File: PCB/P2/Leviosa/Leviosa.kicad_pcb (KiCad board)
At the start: 2 copper layers, 50 parts, among them J1 Barrel_Jack, J2 2.54mm 1x03 Spare

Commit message: finish initial pcb layout
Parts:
- moved H2 128.0 mm to (88.0, 67.0)
- moved H3 98.0 mm to (82.5, 118.5)
- moved H1 70.7 mm to (136.0, 100.0)
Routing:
- net /V_out: track 76.5 -> 85.2 mm
- net /current_sense: track 53.1 -> 57.6 mm
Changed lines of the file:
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@@
 	(footprint "MountingHole:MountingHole_3.2mm_M3_ISO7380"
 		(layer "F.Cu")
-		(at 157.2 174.65)
+		(at 88 67)
 		(descr "Mounting Hole 3.2mm, M3, no annular, generated by kicad-footprint-generator mountinghole.py")
 		(tags "mountinghole M3 ISO7380")
@@
 	(footprint "MountingHole:MountingHole_3.2mm_M3_ISO7380"
 		(layer "F.Cu")
-		(at 157.2 181.9)
+		(at 82.5 118.5)
 		(descr "Mounting Hole 3.2mm, M3, no annular, generated by kicad-footprint-generator mountinghole.py")
 		(tags "mountinghole M3 ISO7380")
@@
 	(footprint "MountingHole:MountingHole_3.2mm_M3_ISO7380"
 		(layer "F.Cu")
-		(at 157.2 167.4)
+		(at 136 100)
 		(descr "Mounting Hole 3.2mm, M3, no annular, generated by kicad-footprint-generator mountinghole.py")
 		(tags "mountinghole M3 ISO7380")
@@
 		(tags "SOD-123")
 		(property "Reference" "D1"
-			(at -3.7 0 0)
+			(at 0 0 0)
 			(layer "F.SilkS")
 			(effects
@@
 	)
 	(segment
+		(start 68 122.37)
+		(end 75.1 129.47)
+		(width 0.25)
+		(layer "F.Cu")
+		(net 2)
+	)
+	(segment
 		(start 75.5 86.85)
 		(end 72.95 84.3)
@@
 	)
 	(segment
+		(start 62.7 110.9)
+		(end 68 116.2)
+		(width 0.25)
+		(layer "F.Cu")
+		(net 2)
+	)
+	(segment
 		(start 129.38 112.0175)
 		(end 129.05 111.6875)
@@
 	(segment
 		(start 67.4 96.5)
-		(end 62.6 101.3)
+		(end 62.7 101.2)
+		(width 0.25)
+		(layer "F.Cu")
+		(net 2)
+	)
+	(segment
+		(start 62.7 101.2)
+		(end 62.7 110.9)
 		(width 0.25)
 		(layer "F.Cu")
@@
 	)
 	(segment
+		(start 68 116.2)
+		(end 68 122.37)
+		(width 0.25)
+		(layer "F.Cu")
+		(net 2)
+	)
+	(segment
 		(start 83.625 124.97)
 		(end 83.625 129.47)
@@
 	)
 	(segment
-		(start 74.47 129.47)
+		(start 75.1 129.47)
 		(end 83.625 129.47)
 		(width 0.25)
@@
 	)
 	(segment
-		(start 62.6 117.6)
-		(end 74.47 129.47)
-		(width 0.25)
-		(layer "F.Cu")
-		(net 2)
-	)
-	(segment
 		(start 118.1 129)
 		(end 109.4 137.7)
@@
 	)
 	(segment
-		(start 62.6 101.3)
-		(end 62.6 117.6)
-		(width 0.25)
-		(layer "F.Cu")
-		(net 2)
-	)
-	(segment
 		(start 97.275 137.7)
 		(end 94.085 134.51)
@@
 	)
 	(segment
-		(start 81.2 68.3)
+		(start 67.9 82.8)
+		(end 67.9 78.6)
+		(width 0.25)
+		(layer "F.Cu")
+		(net 9)
+	)
+	(segment
+		(start 81.435 70.1125)
 		(end 81.435 68.535)
 		(width 0.25)
@@
 	)
 	(segment
+		(start 78.2 68.3)
+		(end 67.9 78.6)
+		(width 0.25)
+		(layer "F.Cu")
+		(net 9)
+	)
+	(segment
 		(start 63.35 91.2)
-		(end 63.35 83.15)
+		(end 63.35 87.35)
 		(width 0.25)
 		(layer "F.Cu")
@@
 	)
 	(segment
-		(start 63.35 83.15)
-		(end 78.2 68.3)
+		(start 63.35 87.35)
+		(end 67.9 82.8)
 		(width 0.25)
 		(layer "F.Cu")
@@
 	)
 	(segment
-		(start 78.2 68.3)
-		(end 81.2 68.3)
+		(start 81.2 68.3)
+		(end 78.2 68.3)
 		(width 0.25)
 		(layer "F.Cu")
@@
 	(segment
 		(start 81.435 68.535)
-		(end 81.435 70.1125)
+		(end 81.2 68.3)
 		(width 0.25)
 		(layer "F.Cu")
@@
 	)
 	(segment
+		(start 77.05 120.05)
+		(end 79.2 122.2)
+		(width 0.4)
+		(layer "F.Cu")
+		(net 11)
+	)
+	(segment
+		(start 111.8 122.2)
+		(end 123.5 110.5)
+		(width 0.4)
+		(layer "F.Cu")
+		(net 11)
+	)
+	(segment
 		(start 73.2 116.188748)
 		(end 70.5 116.188748)
@@
 	)
 	(segment
-		(start 77.05 119.8)
-		(end 77.05 115.55)
+		(start 123.5 110.5)
+		(end 123.5 96.9125)
 		(width 0.4)
 		(layer "F.Cu")
@@
 	)
 	(segment
-		(start 126.6 100.8375)
-		(end 126.6 100.0125)
+		(start 77.05 119.8)
+		(end 77.05 115.55)
 		(width 0.4)
 		(layer "F.Cu")
@@
 	)
 	(segment
-		(start 107.6375 119.8)
-		(end 77.05 119.8)
+		(start 126.6 100.8375)
+		(end 126.6 100.0125)
 		(width 0.4)
 		(layer "F.Cu")
@@
 	)
 	(segment
+		(start 79.2 122.2)
+		(end 111.8 122.2)
+		(width 0.4)
+		(layer "F.Cu")
+		(net 11)
+	)
+	(segment
 		(start 73.888748 115.5)
 		(end 73.2 116.188748)
@@
 	)
 	(segment
-		(start 126.6 100.8375)
-		(end 107.6375 119.8)
+		(start 77.05 119.8)
+		(end 77.05 120.05)
 		(width 0.4)
 		(layer "F.Cu")
@@
 	)
 	(segment
-		(start 127.949 109.308274)
-		(end 127.949 108.18819)
+		(start 110.7 125.4)
+		(end 100.655 125.4)
 		(width 0.25)
 		(layer "F.Cu")
@@
 	)
 	(segment
-		(start 128 108.13719)
-		(end 128 103)
+		(start 127.949 109.308274)
+		(end 127.949 108.18819)
 		(width 0.25)
 		(layer "F.Cu")
@@
 	)
 	(segment
-		(start 128 103)
-		(end 127.6 102.6)
+		(start 100.655 125.4)
+		(end 94.085 131.97)
 		(width 0.25)
 		(layer "F.Cu")
@@
 	)
 	(segment
-		(start 127.6 102.6)
-		(end 125.581376 102.6)
+		(start 128 108.13719)
+		(end 128 103)
 		(width 0.25)
 		(layer "F.Cu")
@@
 	)
 	(segment
-		(start 100.655 125.4)
-		(end 94.085 131.97)
+		(start 125 103.4)
+		(end 125 111.1)
 		(width 0.25)
 		(layer "F.Cu")
@@
 	)
 	(segment
-		(start 102.781376 125.4)
-		(end 100.655 125.4)
+		(start 128 103)
+		(end 127.6 102.6)
 		(width 0.25)
 		(layer "F.Cu")
@@
 	)
 	(segment
-		(start 125.581376 102.6)
-		(end 102.781376 125.4)
+		(start 127.6 102.6)
+		(end 125.8 102.6)
 		(width 0.25)
 		(layer "F.Cu")
@@
 	)
 	(segment
+		(start 125 111.1)
+		(end 110.7 125.4)
+		(width 0.25)
+		(layer "F.Cu")
+		(net 23)
+	)
+	(segment
 		(start 127.874 109.383274)
 		(end 127.949 109.308274)
 		(width 0.25)
 		(layer "F.Cu")
+		(net 23)
+	)
+	(segment
+		(start 125.8 102.6)
+		(end 125 103.4)
+		(width 0.25)
+		(layer "F.Cu")

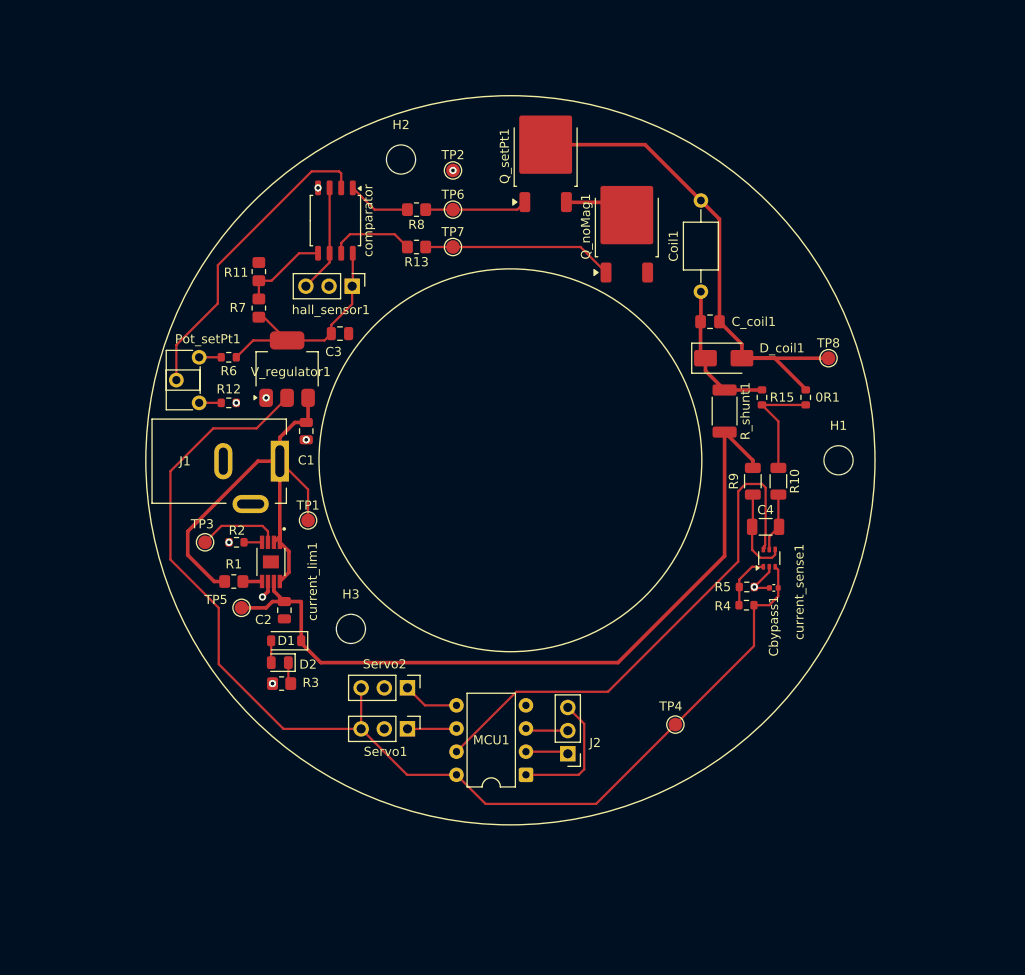
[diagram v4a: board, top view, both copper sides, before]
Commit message: update a resistor and PCB
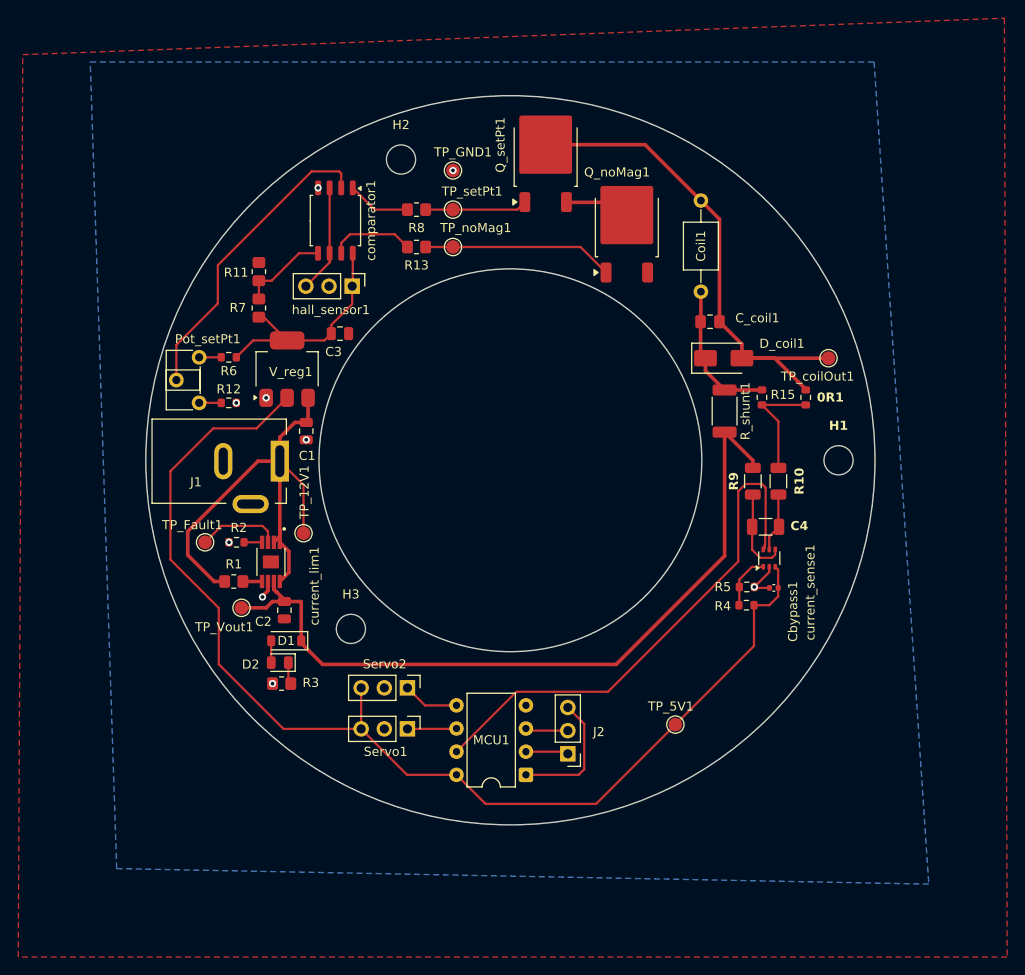
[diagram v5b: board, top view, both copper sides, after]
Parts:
- R11: value 54.2kΩ -> 64.2kΩ
- moved TP_12V1 1.49 mm to (77.3, 108.0)
- renumbered TP1 to TP_12V1, TP4 to TP_5V1, TP3 to TP_Fault1, TP2 to TP_GND1, TP5 to TP_Vout1, TP8 to TP_coilOut1, TP7 to TP_noMag1, TP6 to TP_setPt1, V_regulator1 to V_reg1, comparator to comparator1
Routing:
- net +12V: track 55.5 -> 56.7 mm
- added copper zone on B.Cu, net GND
- added copper zone on F.Cu, net GND
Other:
- board outline added: 80 x 80 mm

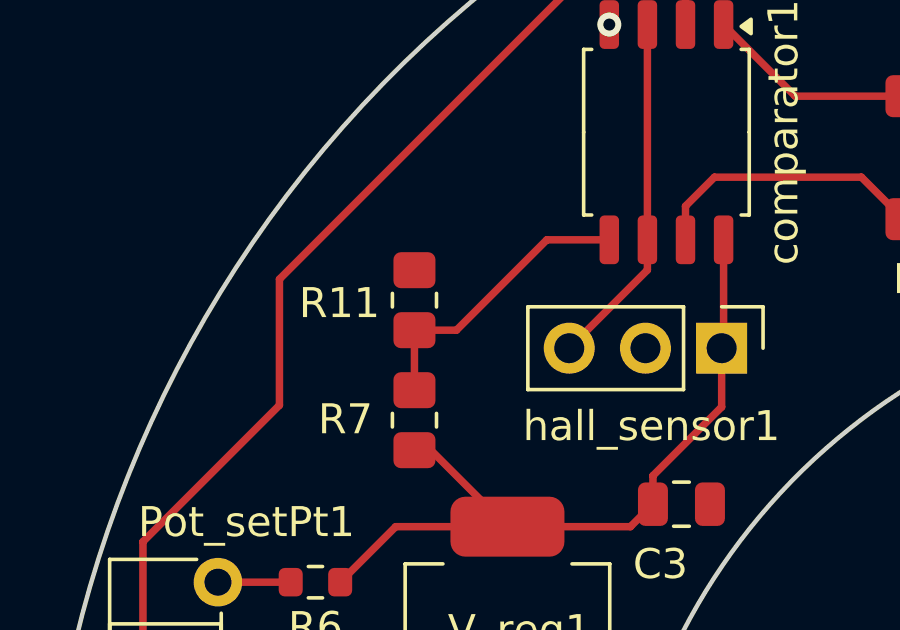
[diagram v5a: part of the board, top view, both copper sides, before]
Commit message: update a resistor footprint
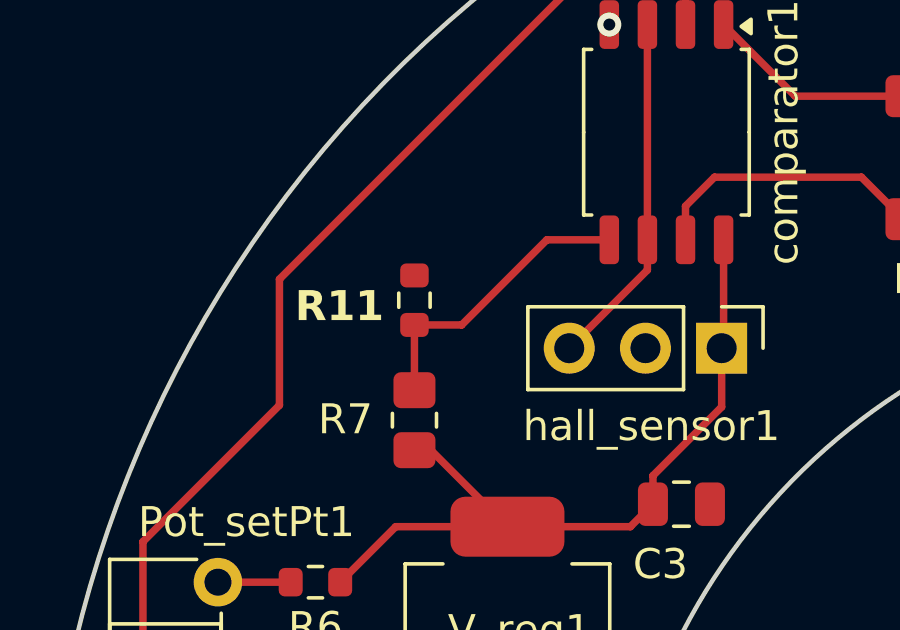
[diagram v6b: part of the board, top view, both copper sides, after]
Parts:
- R11: value 64.2kΩ -> 68kΩ; footprint Resistor_SMD:R_0805_2012Metric_Pad1.20x1.40mm_HandSolder -> Resistor_SMD:R_0603_1608Metric
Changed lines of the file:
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@@
 	(net 30 "Net-(Q_noMag1-G)")
 	(net 31 "Net-(Q_setPt1-G)")
-	(footprint "Resistor_SMD:R_0805_2012Metric_Pad1.20x1.40mm_HandSolder"
+	(footprint "Resistor_SMD:R_0603_1608Metric"
 		(layer "F.Cu")
 		(at 72.4 79.3 -90)
-		(descr "Resistor SMD 0805 (2012 Metric), square (rectangular) end terminal, IPC-7351 nominal with elongated pad for handsoldering. (Body size source: IPC-SM-782 page 72, https://www.pcb-3d.com/wordpress/wp-content/uploads/ipc-sm-782a_amendment_1_and_2.pdf), generated with kicad-footprint-generator")
-		(tags "resistor handsolder")
+		(descr "Resistor SMD 0603 (1608 Metric), square (rectangular) end terminal, IPC-7351 nominal, (Body size source: IPC-SM-782 page 72, https://www.pcb-3d.com/wordpress/wp-content/uploads/ipc-sm-782a_amendment_1_and_2.pdf), generated with kicad-footprint-generator")
+		(tags "resistor")
 		(property "Reference" "R11"
-			(at 0.1 2.5 0)
-			(unlocked yes)
+			(at 0.2 2.5 0)
 			(layer "F.SilkS")
 			(effects
@@
 					(size 1 1)
 					(thickness 0.2)
+					(bold yes)
 				)
 			)
 		)
-		(property "Value" "64.2kΩ"
-			(at 0 1.65 90)
+		(property "Value" "68kΩ"
+			(at 0 1.43 270)
 			(layer "F.Fab")
 			(effects
@@
 		)
 		(property "Datasheet" "~"
-			(at 0 0 90)
+			(at 0 0 270)
 			(layer "F.Fab")
 			(hide yes)
@@
 		)
 		(property "Description" ""
-			(at 0 0 90)
+			(at 0 0 270)
 			(layer "F.Fab")
 			(hide yes)
@@
 			)
 		)
-		(property "Link" ""
+		(property "Link" "https://jlcpcb.com/partdetail/23958-0603WAF6802T5E/C23231"
 			(at 0 0 270)
 			(unlocked yes)
@@
 		(attr smd)
 		(fp_line
-			(start -0.227064 0.735)
-			(end 0.227064 0.735)
+			(start -0.237258 0.5225)
+			(end 0.237258 0.5225)
 			(stroke
 				(width 0.12)
@@
 		)
 		(fp_line
-			(start -0.227064 -0.735)
-			(end 0.227064 -0.735)
+			(start -0.237258 -0.5225)
+			(end 0.237258 -0.5225)
 			(stroke
 				(width 0.12)
@@
 		)
 		(fp_line
-			(start -1.85 0.95)
-			(end -1.85 -0.95)
+			(start -1.48 0.73)
+			(end -1.48 -0.73)
 			(stroke
 				(width 0.05)
@@
 		)
 		(fp_line
-			(start 1.85 0.95)
-			(end -1.85 0.95)
+			(start 1.48 0.73)
+			(end -1.48 0.73)
 			(stroke
 				(width 0.05)
@@
 		)
 		(fp_line
-			(start -1.85 -0.95)
-			(end 1.85 -0.95)
+			(start -1.48 -0.73)
+			(end 1.48 -0.73)
 			(stroke
 				(width 0.05)
@@
 		)
 		(fp_line
-			(start 1.85 -0.95)
-			(end 1.85 0.95)
+			(start 1.48 -0.73)
+			(end 1.48 0.73)
 			(stroke
 				(width 0.05)
@@
 		)
 		(fp_line
-			(start -1 0.625)
-			(end -1 -0.625)
+			(start -0.8 0.4125)
+			(end -0.8 -0.4125)
 			(stroke
 				(width 0.1)
@@
 		)
 		(fp_line
-			(start 1 0.625)
-			(end -1 0.625)
+			(start 0.8 0.4125)
+			(end -0.8 0.4125)
 			(stroke
 				(width 0.1)
@@
 		)
 		(fp_line
-			(start -1 -0.625)
-			(end 1 -0.625)
+			(start -0.8 -0.4125)
+			(end 0.8 -0.4125)
 			(stroke
 				(width 0.1)
@@
 		)
 		(fp_line
-			(start 1 -0.625)
-			(end 1 0.625)
+			(start 0.8 -0.4125)
+			(end 0.8 0.4125)
 			(stroke
 				(width 0.1)
@@
 		)
 		(fp_text user "${REFERENCE}"
-			(at 0 0 90)
-			(unlocked yes)
+			(at 0 0 270)
 			(layer "F.Fab")
 			(effects
 				(font
-					(size 1 1)
-					(thickness 0.15)
+					(size 0.4 0.4)
+					(thickness 0.06)
 				)
 			)
 		)
 		(pad "1" smd roundrect
-			(at -1 0 270)
-			(size 1.2 1.4)
+			(at -0.825 0 270)
+			(size 0.8 0.95)
 			(layers "F.Cu" "F.Mask" "F.Paste")
-			(roundrect_rratio 0.208333)
+			(roundrect_rratio 0.25)
 			(net 3 "GND")
 			(pintype "passive")
 		)
 		(pad "2" smd roundrect
-			(at 1 0 270)
-			(size 1.2 1.4)
+			(at 0.825 0 270)
+			(size 0.8 0.95)
 			(layers "F.Cu" "F.Mask" "F.Paste")
-			(roundrect_rratio 0.208333)
+			(roundrect_rratio 0.25)
 			(net 10 "/no_magnet_point")
 			(pintype "passive")
 		)
 		(embedded_fonts no)
-		(model "${KICAD9_3DMODEL_DIR}/Resistor_SMD.3dshapes/R_0805_2012Metric.step"
+		(model "${KICAD9_3DMODEL_DIR}/Resistor_SMD.3dshapes/R_0603_1608Metric.step"
 			(offset
 				(xyz 0 0 0)
@@
 	)
 	(segment
-		(start 72.4 82.3)
-		(end 72.4 80.3)
+		(start 76.8125 77.2875)
+		(end 78.895 77.2875)
 		(width 0.25)
 		(layer "F.Cu")
@@
 	)
 	(segment
-		(start 78.895 77.2875)
+		(start 73.975 80.125)
 		(end 76.8125 77.2875)
 		(width 0.25)
@@
 	)
 	(segment
-		(start 73.8 80.3)
-		(end 72.4 80.3)
+		(start 72.4 80.125)
+		(end 73.975 80.125)
 		(width 0.25)
 		(layer "F.Cu")
@@
 	)
 	(segment
-		(start 76.8125 77.2875)
-		(end 73.8 80.3)
+		(start 72.4 82.3)
+		(end 72.4 80.125)
 		(width 0.25)
 		(layer "F.Cu")

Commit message: move 5V TP
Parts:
- moved TP_5V1 12.0 mm to (126.5, 120.4)
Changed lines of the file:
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@@
 	(footprint "TestPoint:TestPoint_Pad_D1.5mm"
 		(layer "F.Cu")
-		(at 118.1 129)
+		(at 126.5 120.4)
 		(descr "SMD pad as test Point, diameter 1.5mm")
 		(tags "test point SMD pad")
 		(property "Reference" "TP_5V1"
-			(at -0.5 -2 0)
+			(at -4 -0.7 0)
 			(unlocked yes)
 			(layer "F.SilkS")

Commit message: added cap to attiny and fixed resistors to 8.2R
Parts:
- added C5: 0.1µF, Capacitor_SMD:C_0402_1005Metric, F.Cu at (91.2, 133.9)
- R10: value 8Ω -> 8.2Ω
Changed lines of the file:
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@@
 		(tags "Potentiometer horizontal ACP CA6-H2,5")
 		(property "Reference" "Pot_setPt1"
-			(at -0.95 7 0)
+			(at -0.952 7.086 0)
 			(unlocked yes)
 			(layer "F.SilkS")
@@
 		)
 	)
+	(footprint "Capacitor_SMD:C_0402_1005Metric"
+		(layer "F.Cu")
+		(at 91.186 133.858 90)
+		(descr "Capacitor SMD 0402 (1005 Metric), square (rectangular) end terminal, IPC-7351 nominal, (Body size source: IPC-SM-782 page 76, https://www.pcb-3d.com/wordpress/wp-content/uploads/ipc-sm-782a_amendment_1_and_2.pdf), generated with kicad-footprint-generator")
+		(tags "capacitor")
+		(property "Reference" "C5"
+			(at 0 -1.524 180)
+			(layer "F.SilkS")
+			(effects
+				(font
+					(size 1 1)
+					(thickness 0.2)
+					(bold yes)
+				)
+			)
+		)
+		(property "Value" "0.1µF"
+			(at 0 1.16 90)
+			(layer "F.Fab")
+			(effects
+				(font
+					(size 1 1)
+					(thickness 0.15)
+				)
+			)
+		)
+		(property "Datasheet" "~"
+			(at 0 0 90)
+			(layer "F.Fab")
+			(hide yes)
+			(effects
+				(font
+					(size 1.27 1.27)
+					(thickness 0.15)
+				)
+			)
+		)
+		(property "Description" ""
+			(at 0 0 90)
+			(layer "F.Fab")
+			(hide yes)
+			(effects
+				(font
+					(size 1.27 1.27)
+					(thickness 0.15)
+				)
+			)
+		)
+		(property "Link" "https://jlcpcb.com/partdetail/1877-CL05B104KO5NNNC/C1525"
+			(at 0 0 90)
+			(unlocked yes)
+			(layer "F.Fab")
+			(hide yes)
+			(effects
+				(font
+					(size 1 1)
+					(thickness 0.15)
+				)
+			)
+		)
+		(property ki_fp_filters "C_*")
+		(sheetname "/")
+		(sheetfile "Leviosa.kicad_sch")
+		(attr smd)
+		(fp_line
+			(start -0.107836 -0.36)
+			(end 0.107836 -0.36)
+			(stroke
+				(width 0.12)
+				(type solid)
+			)
+			(layer "F.SilkS")
+		)
+		(fp_line
+			(start -0.107836 0.36)
+			(end 0.107836 0.36)
+			(stroke
+				(width 0.12)
+				(type solid)
+			)
+			(layer "F.SilkS")
+		)
+		(fp_line
+			(start 0.91 -0.46)
+			(end 0.91 0.46)
+			(stroke
+				(width 0.05)
+				(type solid)
+			)
+			(layer "F.CrtYd")
+		)
+		(fp_line
+			(start -0.91 -0.46)
+			(end 0.91 -0.46)
+			(stroke
+				(width 0.05)
+				(type solid)
+			)
+			(layer "F.CrtYd")
+		)
+		(fp_line
+			(start 0.91 0.46)
+			(end -0.91 0.46)
+			(stroke
+				(width 0.05)
+				(type solid)
+			)
+			(layer "F.CrtYd")
+		)
+		(fp_line
+			(start -0.91 0.46)
+			(end -0.91 -0.46)
+			(stroke
+				(width 0.05)
+				(type solid)
+			)
+			(layer "F.CrtYd")
+		)
+		(fp_line
+			(start 0.5 -0.25)
+			(end 0.5 0.25)
+			(stroke
+				(width 0.1)
+				(type solid)
+			)
+			(layer "F.Fab")
+		)
+		(fp_line
+			(start -0.5 -0.25)
+			(end 0.5 -0.25)
+			(stroke
+				(width 0.1)
+				(type solid)
+			)
+			(layer "F.Fab")
+		)
+		(fp_line
+			(start 0.5 0.25)
+			(end -0.5 0.25)
+			(stroke
+				(width 0.1)
+				(type solid)
+			)
+			(layer "F.Fab")
+		)
+		(fp_line
+			(start -0.5 0.25)
+			(end -0.5 -0.25)
+			(stroke
+				(width 0.1)
+				(type solid)
+			)
+			(layer "F.Fab")
+		)
+		(fp_text user "${REFERENCE}"
+			(at 0 0 90)
+			(layer "F.Fab")
+			(effects
+				(font
+					(size 0.25 0.25)
+					(thickness 0.04)
+				)
+			)
+		)
+		(pad "1" smd roundrect
+			(at -0.48 0 90)
+			(size 0.56 0.62)
+			(layers "F.Cu" "F.Mask" "F.Paste")
+			(roundrect_rratio 0.25)
+			(net 2 "/5V")
+			(pintype "passive")
+		)
+		(pad "2" smd roundrect
+			(at 0.48 0 90)
+			(size 0.56 0.62)
+			(layers "F.Cu" "F.Mask" "F.Paste")
+			(roundrect_rratio 0.25)
+			(net 3 "GND")
+			(pintype "passive")
+		)
+		(embedded_fonts no)
+		(model "${KICAD9_3DMODEL_DIR}/Capacitor_SMD.3dshapes/C_0402_1005Metric.step"
+			(offset
+				(xyz 0 0 0)
+			)
+			(scale
+				(xyz 1 1 1)
+			)
+			(rotate
+				(xyz 0 0 0)
+			)
+		)
+	)
 	(footprint "Resistor_SMD:R_0805_2012Metric_Pad1.20x1.40mm_HandSolder"
 		(layer "F.Cu")
@@
 			)
 		)
-		(property "Value" "8Ω"
+		(property "Value" "8.2Ω"
 			(at 0 1.83 90)
 			(layer "F.Fab")
@@
 			)
 		)
+		(property "Link" "https://www.lcsc.com/product-detail/C7467249.html?s_z=n_LR2010-21R050F2"
+			(at 0 0 270)
+			(unlocked yes)
+			(layer "F.Fab")
+			(hide yes)
+			(effects
+				(font
+					(size 1 1)
+					(thickness 0.15)
+				)
+			)
+		)
+		(property "Link2" "https://www.lcsc.com/product-detail/C7467249.html?s_z=n_LR2010-21R050F2"
+			(at 0 0 270)
+			(unlocked yes)
+			(layer "F.Fab")
+			(hide yes)
+			(effects
+				(font
+					(size 1 1)
+					(thickness 0.15)
+				)
+			)
+		)
 		(property ki_fp_filters "R_*")
 		(sheetname "/")
@@
 	)
 	(segment
+		(start 94.085 134.51)
+		(end 91.358 134.51)
+		(width 0.25)
+		(layer "F.Cu")
+		(net 2)
+	)
+	(segment
 		(start 72.15 96.5)
 		(end 67.4 96.5)
@@
 	)
 	(segment
+		(start 88.493 134.338)
+		(end 83.625 129.47)
+		(width 0.25)
+		(layer "F.Cu")
+		(net 2)
+	)
+	(segment
+		(start 91.186 134.338)
+		(end 88.493 134.338)
+		(width 0.25)
+		(layer "F.Cu")
+		(net 2)
+	)
+	(segment
 		(start 75.5 86.85)
 		(end 72.95 84.3)
@@
 	)
 	(segment
-		(start 94.085 134.51)
-		(end 88.665 134.51)
+		(start 91.358 134.51)
+		(end 91.186 134.338)
 		(width 0.25)
 		(layer "F.Cu")
@@
 		(width 0.25)
 		(layer "F.Cu")
-		(net 2)
-	)
-	(segment
-		(start 88.665 134.51)
-		(end 83.625 129.47)
-		(width 0.25)
-		(layer "F.Cu")
